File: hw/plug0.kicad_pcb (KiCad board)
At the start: 2 copper layers, 30 parts, among them U1 pcm3070i, U2 AZ1117C, U3 stm32fxxxz

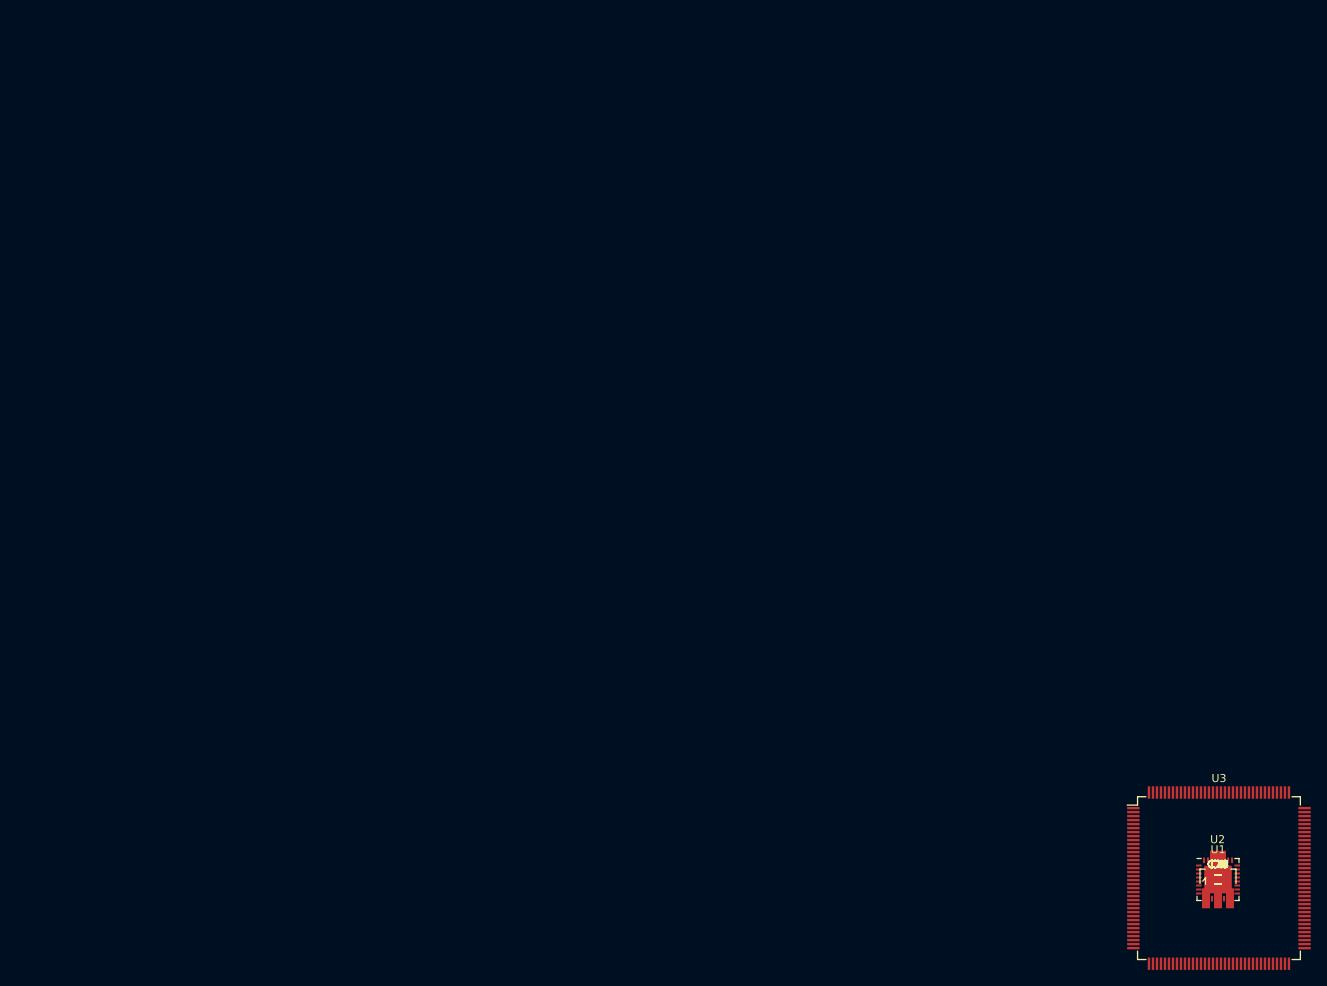
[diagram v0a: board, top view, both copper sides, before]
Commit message: Reorganizada a folha mestre, ajustes nos PN  e criação de folha hierárquica para gestão de bateria e alimentação
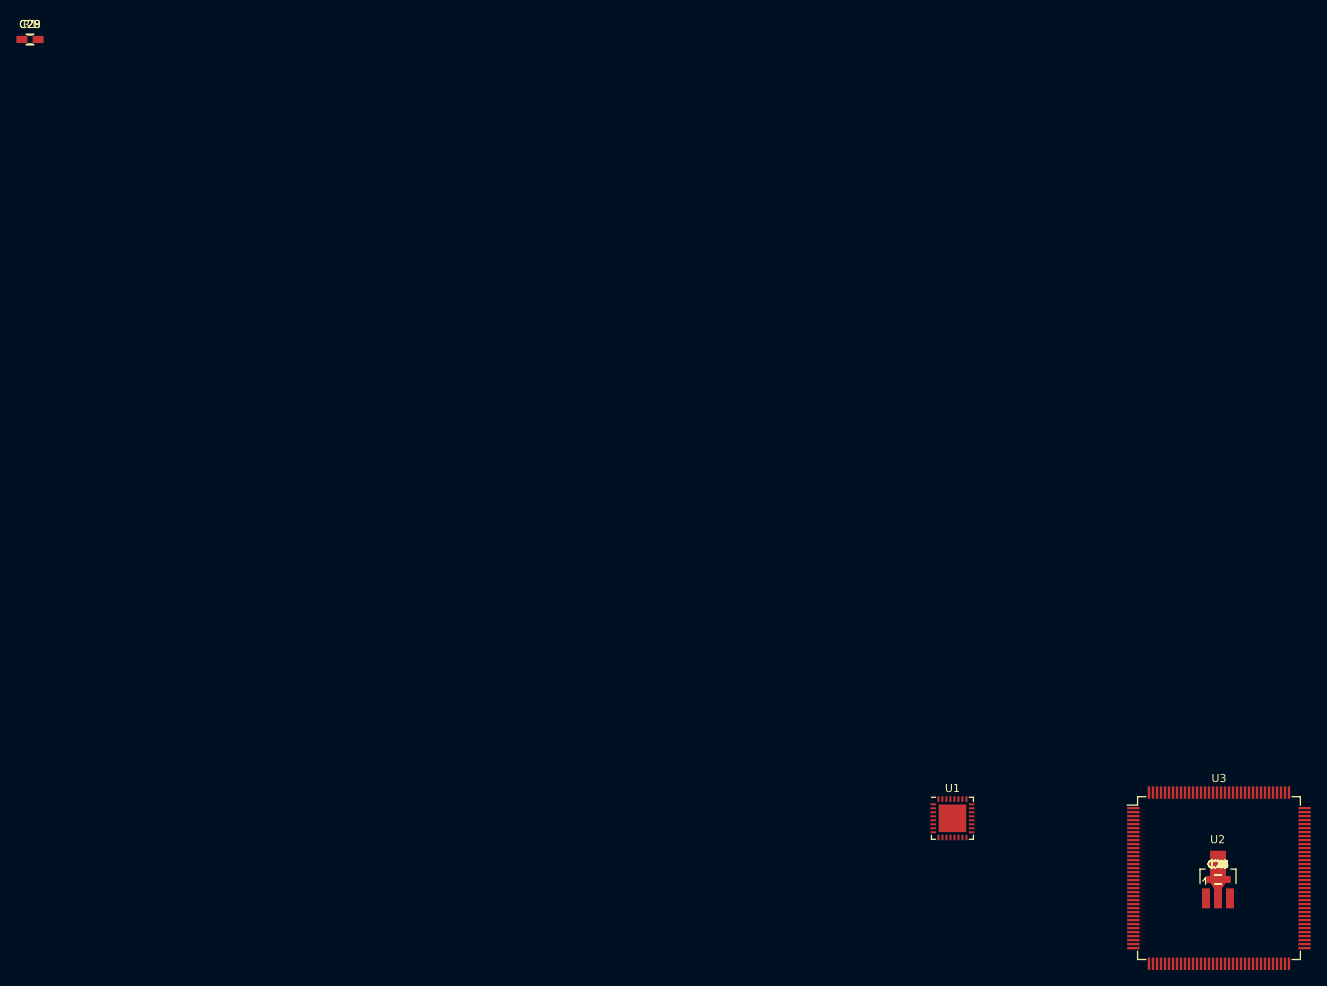
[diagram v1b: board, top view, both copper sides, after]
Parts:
- added C28, C29: 2.2uF, Capacitors_SMD:C_0603, F.Cu at (0.00, 0.00)
- added R1: 10K, Resistors_SMD:R_0603_HandSoldering, F.Cu at (0.00, 0.00)
- moved U1 34.1 mm to (115.3, 97.4)
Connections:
- net /ProcessingUnit/I2S1_CK renamed Net-(U3-Pad41)
- net /ProcessingUnit/I2S1_SD renamed Net-(U3-Pad43)
- net /ProcessingUnit/I2S1_WS renamed Net-(U3-Pad40)
- net Net-(U3-Pad1) renamed /ProcessingUnit/SAI1_MCLK_A
- net Net-(U3-Pad10) renamed /ProcessingUnit/FMC_A0
- net Net-(U3-Pad105) renamed /ProcessingUnit/SWDIO
- net Net-(U3-Pad109) renamed /ProcessingUnit/SWCLK
- net Net-(U3-Pad11) renamed /ProcessingUnit/FMC_A1
- net Net-(U3-Pad112) renamed /ProcessingUnit/SDIO_D3
- net Net-(U3-Pad114) renamed /ProcessingUnit/FMC_D2
- net Net-(U3-Pad115) renamed /ProcessingUnit/FMC_D3
- net Net-(U3-Pad116) renamed /ProcessingUnit/SDIO_CMD
- net Net-(U3-Pad12) renamed /ProcessingUnit/FMC_A2
- net Net-(U3-Pad13) renamed /ProcessingUnit/FMC_A3
- net Net-(U3-Pad132) renamed /ProcessingUnit/~FMC_SDNCAS
- net Net-(U3-Pad14) renamed /ProcessingUnit/FMC_A4
- net Net-(U3-Pad15) renamed /ProcessingUnit/FMC_A5
- net Net-(U3-Pad2) renamed /ProcessingUnit/SAI1_SD_B
- net Net-(U3-Pad25) renamed /ProcessingUnit/~NRST
- net Net-(U3-Pad26) renamed /ProcessingUnit/~FMC_SDNWE
- net Net-(U3-Pad28) renamed /ProcessingUnit/~FMC_SDNE0
- net Net-(U3-Pad29) renamed /ProcessingUnit/FMC_SDCKE0
- net Net-(U3-Pad3) renamed /ProcessingUnit/SAI1_FS_A
- net Net-(U3-Pad4) renamed /ProcessingUnit/SAI1_SCK_A
- net Net-(U3-Pad49) renamed /ProcessingUnit/~FMC_SDNRAS
- net Net-(U3-Pad5) renamed /ProcessingUnit/SAI1_SD_A
- net Net-(U3-Pad50) renamed /ProcessingUnit/FMC_A6
- net Net-(U3-Pad53) renamed /ProcessingUnit/FMC_A7
- net Net-(U3-Pad54) renamed /ProcessingUnit/FMC_A8
- net Net-(U3-Pad55) renamed /ProcessingUnit/FMC_A9
- net Net-(U3-Pad56) renamed /ProcessingUnit/FMC_A10
- net Net-(U3-Pad57) renamed /ProcessingUnit/FMC_A11
- net Net-(U3-Pad58) renamed /ProcessingUnit/FMC_D4
- net Net-(U3-Pad59) renamed /ProcessingUnit/FMC_D5
- net Net-(U3-Pad60) renamed /ProcessingUnit/FMC_D6
- net Net-(U3-Pad63) renamed /ProcessingUnit/FMC_D7
- net Net-(U3-Pad64) renamed /ProcessingUnit/FMC_D8
- net Net-(U3-Pad65) renamed /ProcessingUnit/FMC_D9
- net Net-(U3-Pad66) renamed /ProcessingUnit/FMC_D10
- net Net-(U3-Pad67) renamed /ProcessingUnit/FMC_D11
- net Net-(U3-Pad68) renamed /ProcessingUnit/FMC_D12
- net Net-(U3-Pad85) renamed /ProcessingUnit/FMC_D0
- net Net-(U3-Pad86) renamed /ProcessingUnit/FMC_D1
- net Net-(U3-Pad89) renamed /ProcessingUnit/FMC_BA0
- net Net-(U3-Pad93) renamed /ProcessingUnit/FMC_SDCLK
- net Net-(U3-Pad98) renamed /ProcessingUnit/SDIO_D0
- U3 pad 107: Net-(U3-Pad107) -> GND
- U3 pad 108: Net-(U3-Pad108) -> VDD
- U3 pad 120: Net-(U3-Pad120) -> GND
- U3 pad 121: Net-(U3-Pad121) -> VDD
- U3 pad 127: /ProcessingUnit/FMC_D13 -> Net-(U3-Pad127)
- U3 pad 128: /ProcessingUnit/FMC_D14 -> Net-(U3-Pad128)
- U3 pad 129: /ProcessingUnit/FMC_D15 -> Net-(U3-Pad129)
- U3 pad 130: Net-(U3-Pad130) -> GND
- U3 pad 131: Net-(U3-Pad131) -> VDD
- U3 pad 143: Net-(U3-Pad143) -> VDD
- U3 pad 144: Net-(U3-Pad144) -> VDD
- U3 pad 16: Net-(U3-Pad16) -> GND
- U3 pad 17: Net-(U3-Pad17) -> VDD
- U3 pad 23: Net-(U3-Pad23) -> Net-(C27-Pad1)
- U3 pad 24: Net-(U3-Pad24) -> Net-(C26-Pad1)
- U3 pad 30: Net-(U3-Pad30) -> VDD
- U3 pad 31: Net-(U3-Pad31) -> GND
- U3 pad 32: Net-(U3-Pad32) -> VAA
- U3 pad 33: Net-(U3-Pad33) -> VAA
- U3 pad 38: Net-(U3-Pad38) -> GND
- U3 pad 39: Net-(U3-Pad39) -> VDD
- U3 pad 51: Net-(U3-Pad51) -> GND
- U3 pad 52: Net-(U3-Pad52) -> VDD
- U3 pad 6: Net-(U3-Pad6) -> VDD
- U3 pad 61: Net-(U3-Pad61) -> GND
- U3 pad 62: Net-(U3-Pad62) -> VDD
- U3 pad 72: Net-(U3-Pad72) -> VDD
- U3 pad 77: Net-(U3-Pad77) -> /ProcessingUnit/FMC_D13
- U3 pad 78: Net-(U3-Pad78) -> /ProcessingUnit/FMC_D14
- U3 pad 79: Net-(U3-Pad79) -> /ProcessingUnit/FMC_D15
- U3 pad 83: Net-(U3-Pad83) -> GND
- U3 pad 84: Net-(U3-Pad84) -> VDD
- U3 pad 94: Net-(U3-Pad94) -> GND
- U3 pad 95: Net-(U3-Pad95) -> VDD
